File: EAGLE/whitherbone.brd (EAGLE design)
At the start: 86.4 x 54.6 mm, 220 parts, among them IC1 A4983, IC12 TPS2051BDGN, IC13 SN74AUC1G74, IC14 TPD4S012DRY, IC15 TPD4S012DRY, IC17 SN74LVC2G241DCUR, IC2 SN74LVC1G07DCK, IC4 7805T, IC7 IP4283CZ10-TBR, IC8 IP4283CZ10-TBR, IC9 TDA19988BHN/C1,557, J1 1-1747981-1, Q2 32.768kHz, Q4 24 MHz, T1 BSS138W-7-F, T3 BSS138W-7-F, T4 BSS138W-7-F, U1 OSD3358-512M-BSM, U2 SN74AHCT125PW, X2 SCHA5B0200, X4 10118192-0001LF

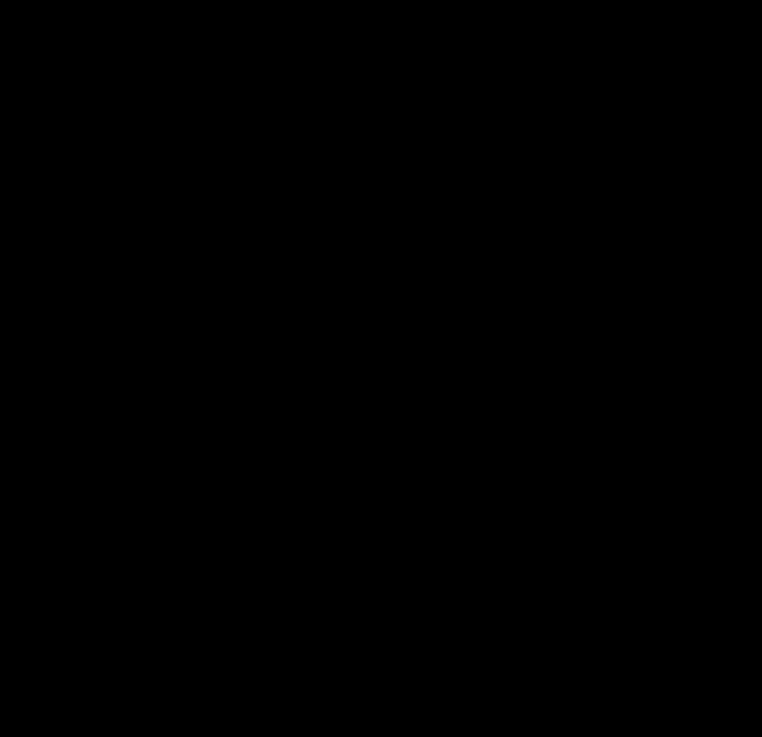
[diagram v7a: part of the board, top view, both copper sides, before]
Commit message: Add quick fan connector
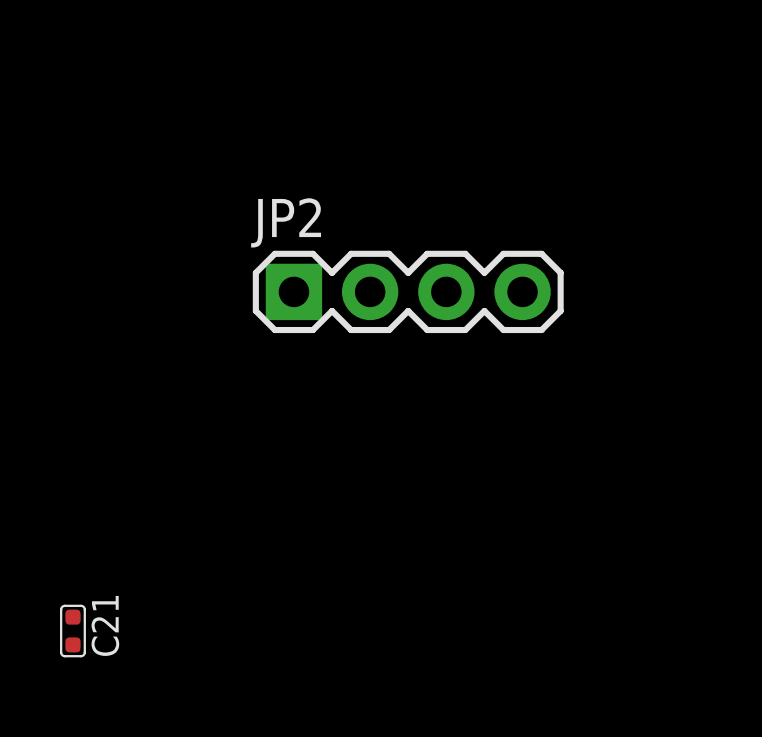
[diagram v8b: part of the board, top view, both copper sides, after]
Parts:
- added C21: 1uF,10V, Seeed-Capacitor:C0402
- added JP2: (no value), SparkFun:1X04
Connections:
- net GND: now also JP1.4, JP2.1, JP2.4
- net VDD_5V: now also JP1.2, JP2.2, JP2.3; no longer JP1.4
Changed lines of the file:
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@@
 <attribute name="MPN" value="CC0402KRX5R6BB105" x="-76.4286" y="-248.285" size="1.778" layer="27" display="off"/>
+</element>
+<element name="JP2" library="SparkFun" package="1X04" value="" x="-69.0626" y="-261.1628"/>
+<element name="C21" library="Seeed-Capacitor" package="C0402" value="1uF,10V" x="-76.4286" y="-272.4658">
+<attribute name="MPN" value="CC0402KRX5R6BB105" x="-80.391" y="-267.081" size="1.778" layer="27" display="off"/>
 </element>
 </elements>
@@
 <contactref element="U2" pad="9"/>
 <contactref element="U2" pad="12"/>
+<contactref element="JP2" pad="1"/>
+<contactref element="JP1" pad="4"/>
+<contactref element="JP2" pad="4"/>
 <wire x1="-53.2996" y1="-153.3144" x2="-56.3984" y2="-153.3144" width="0" layer="19" extent="1-1"/>
 <wire x1="-50.2008" y1="-153.3144" x2="-53.2996" y2="-153.3144" width="0" layer="19" extent="1-1"/>
@@
 <wire x1="-60.1044" y1="-210.1088" x2="-53.2996" y2="-156.4894" width="0" layer="19" extent="1-1"/>
 <wire x1="-52.3494" y1="-242.3668" x2="-60.1044" y2="-210.1088" width="0" layer="19" extent="1-1"/>
+<wire x1="-44.7294" y1="-242.3668" x2="-52.3494" y2="-242.3668" width="0" layer="19" extent="1-1"/>
 <wire x1="-65.2018" y1="-244.8052" x2="-52.3494" y2="-242.3668" width="0" layer="19" extent="1-1"/>
 <wire x1="-65.2018" y1="-246.761" x2="-65.2018" y2="-244.8052" width="0" layer="19" extent="1-1"/>
@@
 <wire x1="-71.0438" y1="-246.126" x2="-71.0438" y2="-247.4214" width="0" layer="19" extent="1-1"/>
 <wire x1="-71.0438" y1="-243.5098" x2="-71.0438" y2="-246.126" width="0" layer="19" extent="1-1"/>
+<wire x1="-69.0626" y1="-261.1628" x2="-71.0438" y2="-247.4214" width="0" layer="19" extent="1-1"/>
+<wire x1="-61.4426" y1="-261.1628" x2="-69.0626" y2="-261.1628" width="0" layer="19" extent="1-1"/>
 <wire x1="-46.857" y1="-85.0646" x2="-49.9266" y2="-145.0848" width="0" layer="19" extent="1-1"/>
 <wire x1="-30.211" y1="-72.9844" x2="-46.857" y2="-85.0646" width="0" layer="19" extent="1-1"/>
@@
 <contactref element="U1" pad="R10"/>
 <contactref element="U1" pad="T10"/>
-<contactref element="JP1" pad="4"/>
 <contactref element="U2" pad="14"/>
 <contactref element="U2" pad="4"/>
 <contactref element="U2" pad="10"/>
 <contactref element="U2" pad="13"/>
+<contactref element="JP1" pad="2"/>
+<contactref element="JP2" pad="2"/>
+<contactref element="JP2" pad="3"/>
 <wire x1="60.7568" y1="72.4916" x2="62.0268" y2="72.4916" width="0" layer="19" extent="1-1"/>
 <wire x1="59.4868" y1="72.4916" x2="60.7568" y2="72.4916" width="0" layer="19" extent="1-1"/>
 <wire x1="-24.6888" y1="-39.2176" x2="59.4868" y2="72.4916" width="0" layer="19" extent="1-1"/>
-<wire x1="-44.7294" y1="-242.3668" x2="-24.6888" y2="-39.2176" width="0" layer="19" extent="1-1"/>
-<wire x1="-65.2018" y1="-243.5098" x2="-44.7294" y2="-242.3668" width="0" layer="19" extent="1-1"/>
+<wire x1="-49.8094" y1="-242.3668" x2="-24.6888" y2="-39.2176" width="0" layer="19" extent="1-1"/>
+<wire x1="-65.2018" y1="-243.5098" x2="-49.8094" y2="-242.3668" width="0" layer="19" extent="1-1"/>
 <wire x1="-65.2018" y1="-244.1702" x2="-65.2018" y2="-243.5098" width="0" layer="19" extent="1-1"/>
 <wire x1="-65.2018" y1="-246.126" x2="-65.2018" y2="-244.1702" width="0" layer="19" extent="1-1"/>
 <wire x1="-71.0438" y1="-245.4656" x2="-65.2018" y2="-246.126" width="0" layer="19" extent="1-1"/>
+<wire x1="-66.5226" y1="-261.1628" x2="-65.2018" y2="-246.126" width="0" layer="19" extent="1-1"/>
+<wire x1="-63.9826" y1="-261.1628" x2="-66.5226" y2="-261.1628" width="0" layer="19" extent="1-1"/>
 </signal>
 <signal name="PWR_BUT">
